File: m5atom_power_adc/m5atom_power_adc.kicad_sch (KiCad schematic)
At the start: 68 parts, among them J101 USB_C_Receptacle_USB2.0_16P, J102 Conn_01x04_Pin, J103 SubBatt, J104 MainBatt, J105 I2C, J106 Shunt, Q101 AO3401A, Q102 MMBT2222A, Q103 AO3401A, SW101 Boot, SW102 Reset, SW103 Btn0, SW104 Btn1, U101 LM2596S-5, U102 AMS1117-3.3, U103 ESP32-S3-MINI-1, U104 AMS1117-3.3, U105 LTC2944, U106 ADS1115IDGS, U108 INA228

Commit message: chore: Grove LED色変更・リレー抵抗を680Ω 500mWに変更・INA228品番更新
Co-Authored-By: Claude Sonnet 4.6 <noreply@anthropic.com>
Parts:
- C112: LCSC C5199872 -> C14663
- R104: value 1k -> 200; LCSC C21190 -> C8218
- U108: LCSC C2862904 -> C2887910
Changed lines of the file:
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@@
 			)
 		)
-		(property "LCSC" "C2862904"
+		(property "LCSC" "C2887910"
 			(at 341.63 45.72 0)
 			(effects
@@
 			)
 		)
-		(property "Value" "1k"
+		(property "Value" "200"
 			(at 132.08 39.37 90)
 			(effects
@@
 			)
 		)
-		(property "LCSC" "C21190"
+		(property "LCSC" "C8218"
 			(at 132.08 41.91 90)
 			(effects
@@
 			)
 		)
-		(property "LCSC" "C5199872"
+		(property "LCSC" "C14663"
 			(at 363.22 34.29 0)
 			(effects

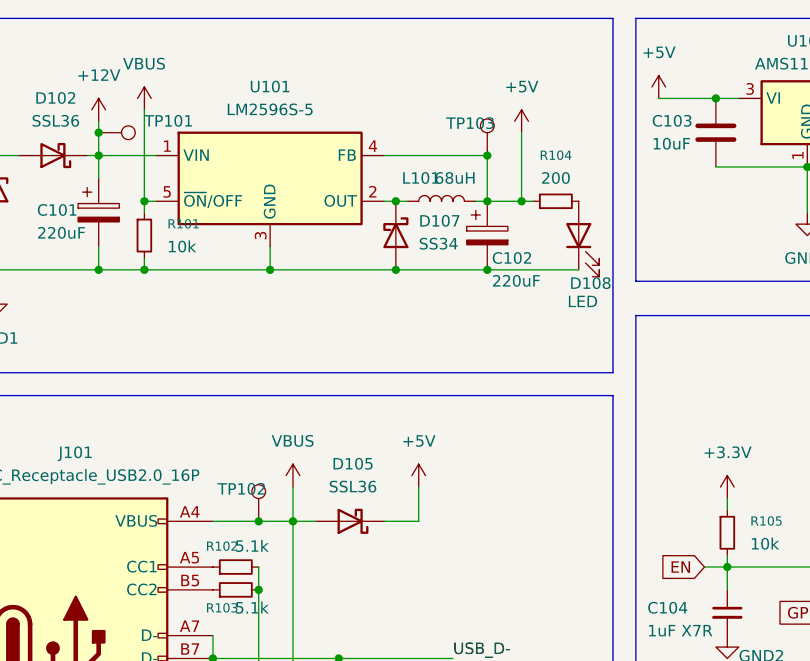
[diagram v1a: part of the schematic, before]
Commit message: feat: m5atom_power_adc 回路・PCB を更新
KiCad 上で行った回路設計・PCB レイアウト変更を反映。
変更内容の詳細は KiCad 上で差分を確認すること。

Co-Authored-By: Claude Sonnet 4.6 <noreply@anthropic.com>
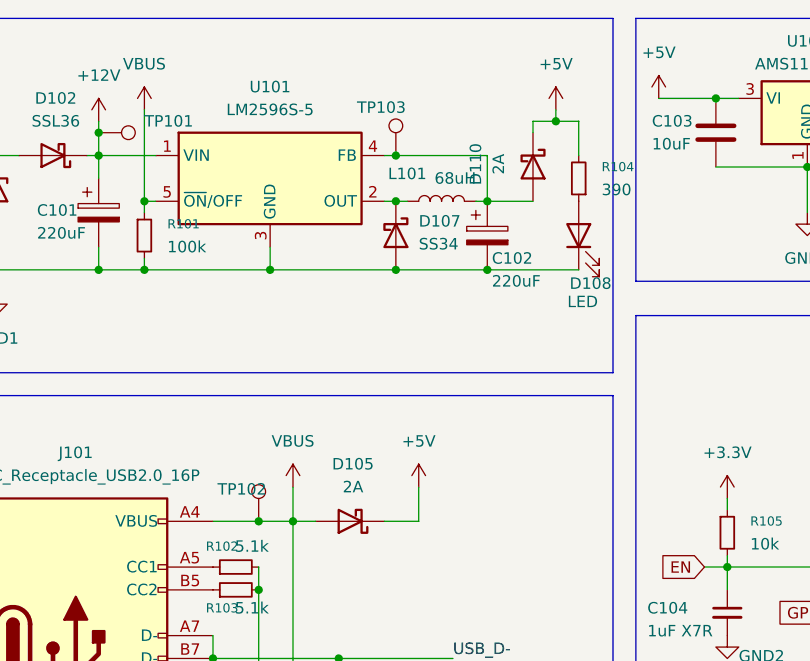
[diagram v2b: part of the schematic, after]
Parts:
- added D110: 2A, Diode_SMD:D_SOD-123F, symbol Device:D_Schottky
- D105: value SSL36 -> 2A; footprint Diode_SMD:D_SMA -> Diode_SMD:D_SOD-123F; LCSC C28646286 -> C496544
- R101: value 10k -> 100k; footprint Resistor_SMD:R_0402_1005Metric -> Resistor_SMD:R_0603_1608Metric; LCSC C2906862 -> C25803
- R102, R103: LCSC C2907045 -> C23186
- R104: value 200 -> 390; LCSC C8218 -> C23151
- R105, R108, R109, R111, R112, R113: footprint Resistor_SMD:R_0402_1005Metric -> Resistor_SMD:R_0603_1608Metric; LCSC C2906862 -> C25804
- R106: LCSC C2906981 -> C25803
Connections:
- net +5V: now also R104.2, D110.1 (K); no longer C102.1, L101.2, R104.1, TP103.1, U101.4 (FB)
- net at D108.2 (A): now also R104.1; no longer R104.2
- new net: C102.1, D110.2 (A), L101.2, TP103.1, U101.4 (FB)
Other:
- moved on the sheet: R104, TP103

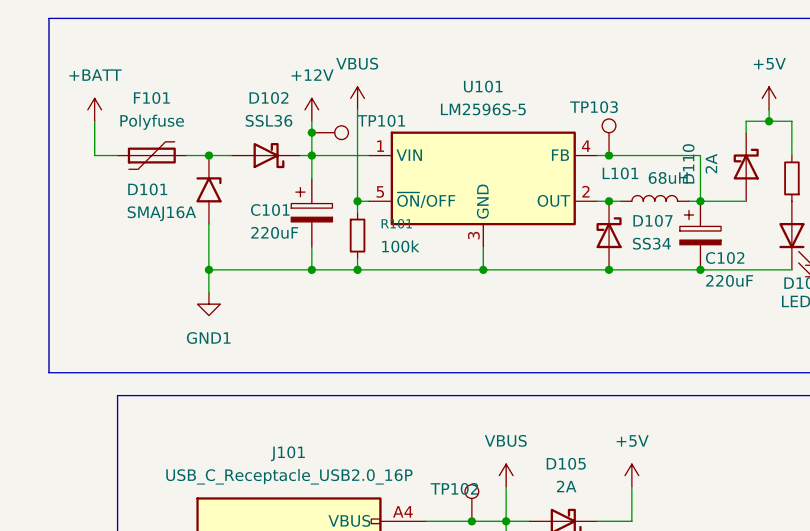
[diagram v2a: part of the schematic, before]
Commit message: fix: R1を100kΩから1kΩに変更（SBD逆方向漏れによる/EN誤動作対策）
SBDの逆方向電流はVR=5V付近でも最大500μAに達するフラット特性のため、
100kΩではV_/EN=5Vとなり/ENしきい値を超えてDCDCが発振する。
1kΩに変更することでV_/EN≤0.5V（25°C）を確保。
LCSC部品番号をC25803→C21190に更新。

Co-Authored-By: Claude Sonnet 4.6 <noreply@anthropic.com>
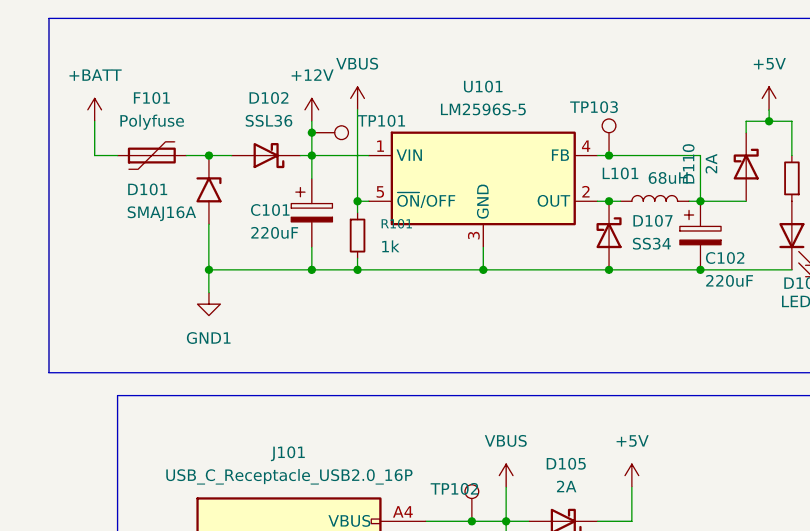
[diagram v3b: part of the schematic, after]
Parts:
- R101: value 100k -> 1k; LCSC C25803 -> C21190
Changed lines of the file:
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@@
 			)
 		)
-		(property "Value" "100k"
+		(property "Value" "1k"
 			(at 88.9 46.9899 0)
 			(effects
@@
 			)
 		)
-		(property "LCSC" "C25803"
+		(property "LCSC" "C21190"
 			(at 86.36 45.72 0)
 			(effects

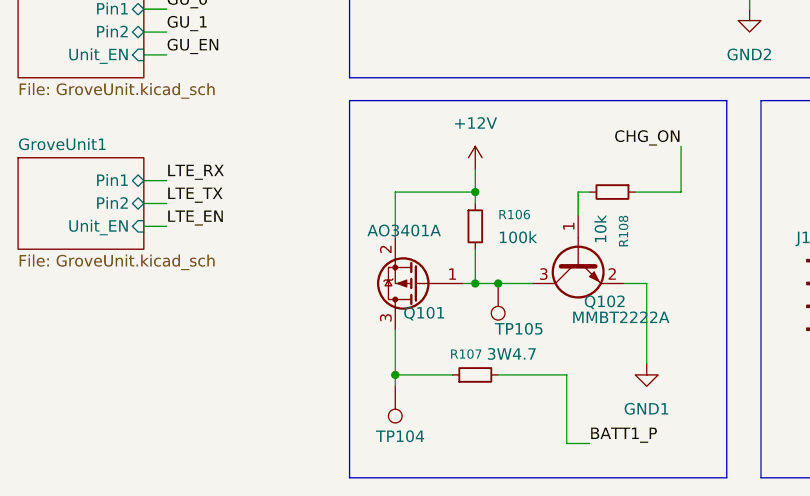
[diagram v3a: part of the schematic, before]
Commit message: feat: 緊急充電回路をバイポーラトランジスタ構成に変更
P-ch MOSFET（AO3401A）をPNPトランジスタに置き換え、ボディダイオードによる
逆電流を防止。ベース電流制限抵抗（R114 470Ω）を追加しQ102の過熱を防ぐ。

Co-Authored-By: Claude Sonnet 4.6 <noreply@anthropic.com>
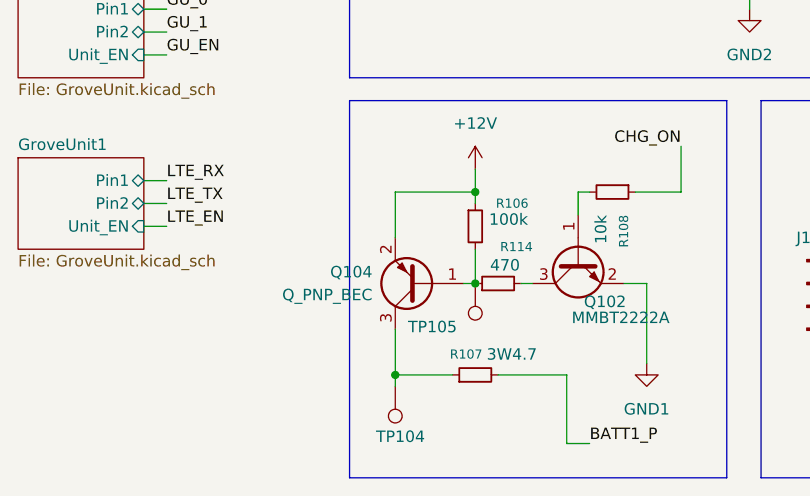
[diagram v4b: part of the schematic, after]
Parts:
- removed Q101: AO3401A, Package_TO_SOT_SMD:SOT-23, symbol Transistor_FET:AO3401A
- added Q104: Q_PNP_BEC, Package_TO_SOT_SMD:SOT-23, symbol Transistor_BJT:Q_PNP_BEC
- added R114: 470, Resistor_SMD:R_0603_1608Metric, symbol Device:R_Small
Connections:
- net +12V: now also Q104.2 (E)
- net at R106.2, TP105.1: now also Q104.1 (B), R114.1; no longer Q102.3 (C)
- net at R107.1, TP104.1: now also Q104.3 (C)
- new net: Q102.3 (C), R114.2
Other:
- moved on the sheet: TP105

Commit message: chore: m5atom_power_adc LCSC 品番を更新
Co-Authored-By: Claude Sonnet 4.6 <noreply@anthropic.com>
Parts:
- Q104: LCSC C8326 -> C7420371
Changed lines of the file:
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@@
 			)
 		)
-		(property "LCSC" "C8326"
+		(property "LCSC" "C7420371"
 			(at 148.59 171.45 0)
 			(effects

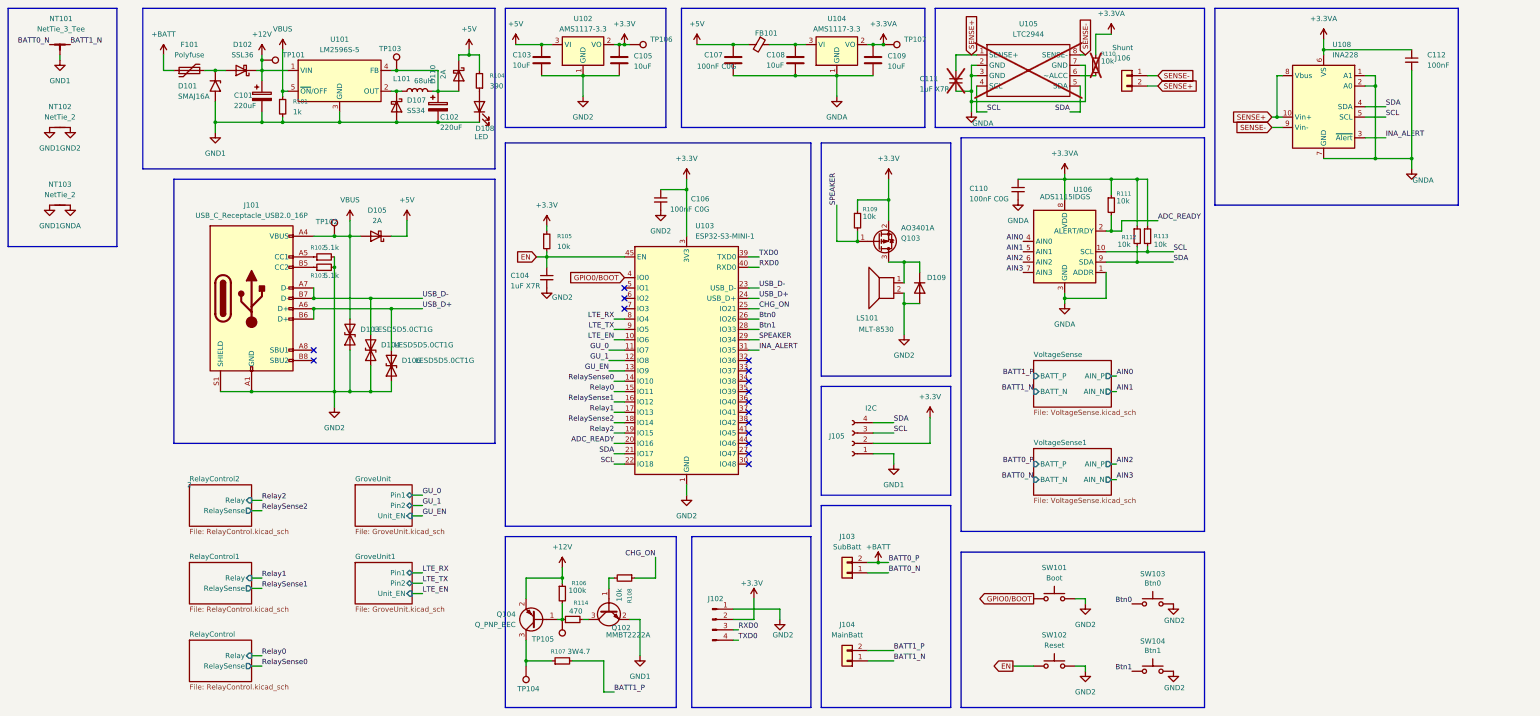
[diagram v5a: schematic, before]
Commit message: feat(m5atom_power_adc): 逆極性保護を理想ダイオード(LM73100)に置き換え、電源スイッチ＆自己保持回路を追加（作業途中）
- LM73100用カスタム記号・フットプリント(VQFN-10-HR)を追加
- 電源回路をサブシートに分離(power.kicad_sch)
- PCBレイアウト更新

Co-Authored-By: Claude Sonnet 4.6 <noreply@anthropic.com>
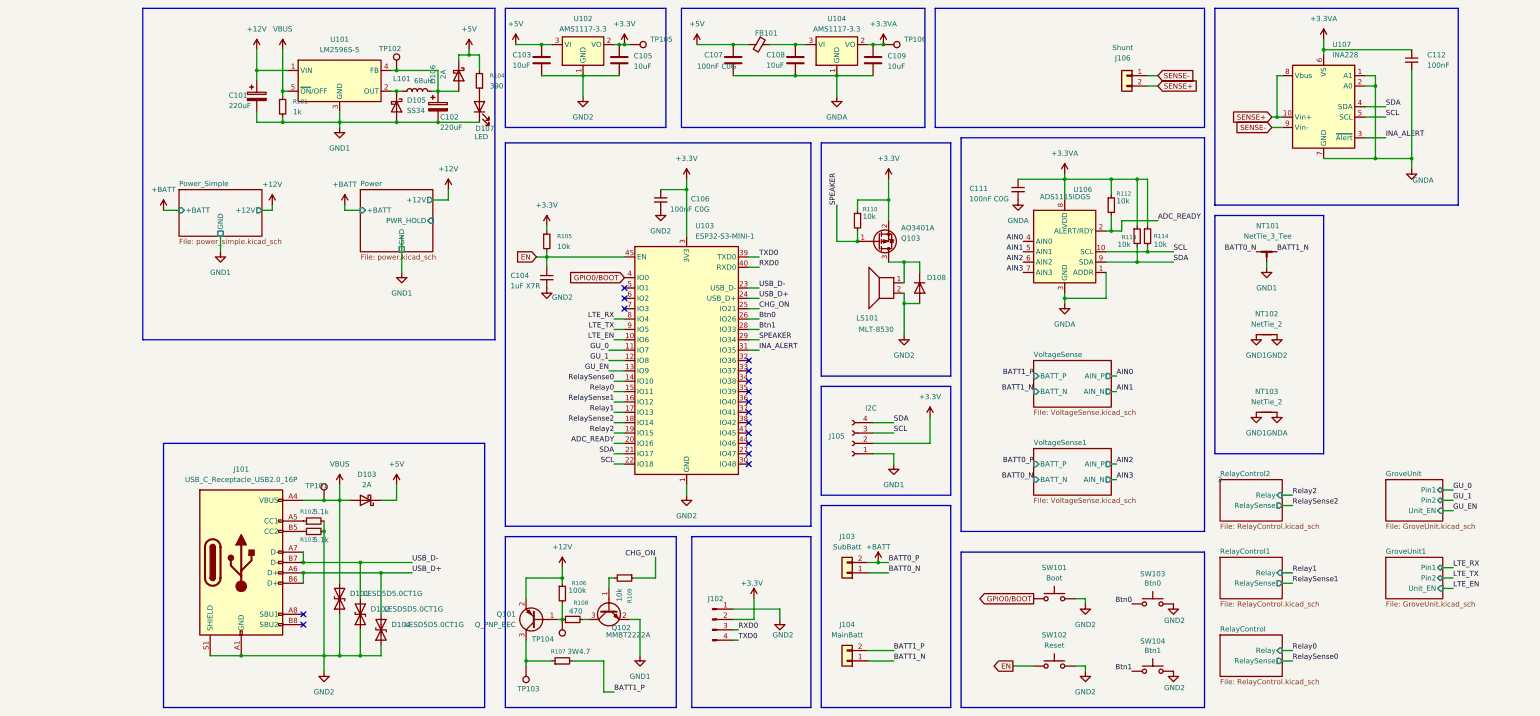
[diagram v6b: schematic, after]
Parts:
- removed C111: 1uF X7R, Capacitor_SMD:C_0603_1608Metric, symbol Device:C_Small
- removed D101: SMAJ16A, Diode_SMD:D_SMB, symbol Diode:SMAJ16A
- removed D102: SSL36, Diode_SMD:D_SMA, symbol Device:D_Schottky
- removed F101: Polyfuse, Fuse:Fuse_1812_4532Metric, symbol Device:Polyfuse
- removed R110: 10k, Resistor_SMD:R_0402_1005Metric, symbol Device:R_Small
- removed TP101: TestPoint, TestPoint:TestPoint_Pad_D1.5mm, symbol Connector:TestPoint
- removed U105: LTC2944, Package_DFN_QFN:DFN-8-1EP_3x3mm_P0.5mm_EP1.65x2.38mm, symbol 000_my:LTC2944
- renumbered C110 to C111, D103 to D101, D104 to D102, D105 to D103, D106 to D104, D107 to D105, D110 to D106, D108 to D107, D109 to D108, Q104 to Q101, R114 to R108, R108 to R109, R109 to R110, R111 to R112, R112 to R113, R113 to R114, TP102 to TP101, TP103 to TP102, TP104 to TP103, TP105 to TP104, TP106 to TP105, TP107 to TP106, U108 to U107
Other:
- added sheet Power (power.kicad_sch)
- added sheet Power_Simple (power_simple.kicad_sch)
- moved on the sheet: C101, D101, D102, D103, D104, J101, NT101, NT102, NT103, R102, R103, TP101

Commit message: feat(m5atom_power_adc): リレー状態検出をアナログ分圧からI2C入力に変更
- 分圧抵抗(R201/R202/R301/R302/R401/R402)とRelaySenseラベルを削除
- I2Cコネクタ(J107/J108)を追加、GP2/GP3/GP11/GP12・PWR_HOLDラベルを追加
- +12VAラベルを+12VRAWにリネーム
- ネットクラスの配線幅プリセットに1.0mmを追加
- PCBのネット再割当て・DRC警告を解消

Co-Authored-By: Claude Sonnet 5 <noreply@anthropic.com>
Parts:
- added J107, J108: I2C, 000_Local:HY2.0-4PZZ, symbol Connector:Conn_01x04_Socket
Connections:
- net RelaySense2 is gone; now on net Relay1: U103.18 (IO14)
- net +3.3V: now also J107.2 (Pin_2), J108.2 (Pin_2)
- net GND1: now also J108.1 (Pin_1)
- net GND2: now also J107.1 (Pin_1)
- net Relay0: now also U103.17 (IO13); no longer U103.15 (IO11)
- net Relay1: no longer U103.17 (IO13)
- net GP2: now reaches U103.6 (IO2)
- net GP2: now also J108.4 (Pin_4)
- net GP3: now reaches U103.7 (IO3)
- net GP3: now also J108.3 (Pin_3)
- net RelaySense0 renamed PWR_HOLD
- net RelaySense1 renamed GP12
- net GP12: now also J107.4 (Pin_4)
- new net GP11: J107.3 (Pin_3), U103.15 (IO11)
- no-connect marks 16 -> 14
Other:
- sheet RelayControl ports: added none; removed RelaySense
- sheet RelayControl1 ports: added none; removed RelaySense
- sheet RelayControl2 ports: added none; removed RelaySense

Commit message: refactor(m5atom_power_adc): Grove Unitのネットラベルをシルク表記に統一
- LTE_RX/TX/EN・GU_0/1/ENをGU1_0/1/EN・GU0_0/1/ENにリネーム
- 基板シルクの「GU0」「GU1」表記に合わせ、CIRCUIT.mdの記載と整合させる

Co-Authored-By: Claude Sonnet 5 <noreply@anthropic.com>
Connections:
- net LTE_EN: no longer U103.10 (IO6)
- net LTE_RX: no longer U103.8 (IO4)
- net LTE_TX: no longer U103.9 (IO5)
- net GU_0 renamed GU1_0
- net GU_1 renamed GU1_1
- net GU_EN renamed GU1_EN
- new net GU0_0: U103.8 (IO4)
- new net GU0_1: U103.9 (IO5)
- new net GU0_EN: U103.10 (IO6)
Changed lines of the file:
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@@
 	(wire
 		(pts
-			(xy 373.38 158.75) (xy 370.84 158.75)
-		)
-		(stroke
-			(width 0)
-			(type default)
-		)
-	)
-	(wire
-		(pts
 			(xy 242.57 86.36) (xy 242.57 83.82)
 		)
@@
 	(wire
 		(pts
+			(xy 370.84 158.75) (xy 373.38 158.75)
+		)
+		(stroke
+			(width 0)
+			(type default)
+		)
+	)
+	(wire
+		(pts
 			(xy 105.41 157.48) (xy 118.11 157.48)
 		)
@@
 	(wire
 		(pts
+			(xy 370.84 163.83) (xy 373.38 163.83)
+		)
+		(stroke
+			(width 0)
+			(type default)
+		)
+	)
+	(wire
+		(pts
 			(xy 238.76 83.82) (xy 234.95 83.82)
 		)
@@
 	(wire
 		(pts
-			(xy 373.38 163.83) (xy 370.84 163.83)
-		)
-		(stroke
-			(width 0)
-			(type default)
-		)
-	)
-	(wire
-		(pts
 			(xy 110.49 160.02) (xy 118.11 160.02)
 		)
@@
 	(wire
 		(pts
-			(xy 373.38 161.29) (xy 370.84 161.29)
-		)
-		(stroke
-			(width 0)
-			(type default)
-		)
-	)
-	(wire
-		(pts
 			(xy 363.22 36.83) (xy 363.22 58.42)
 		)
@@
 	(wire
 		(pts
+			(xy 370.84 161.29) (xy 373.38 161.29)
+		)
+		(stroke
+			(width 0)
+			(type default)
+		)
+	)
+	(wire
+		(pts
 			(xy 330.2 38.1) (xy 331.47 38.1)
 		)
@@
 		)
 	)
+	(label "GU0_EN"
+		(at 167.64 102.87 180)
+		(effects
+			(font
+				(size 1.27 1.27)
+			)
+			(justify right bottom)
+		)
+	)
 	(label "Relay0"
 		(at 334.01 179.07 0)
@@
 		)
 	)
-	(label "GU_EN"
+	(label "GU1_EN"
 		(at 373.38 144.78 0)
 		(effects
@@
 		)
 	)
-	(label "GU_EN"
+	(label "GU1_EN"
 		(at 167.64 110.49 180)
 		(effects
@@
 		)
 	)
-	(label "GU_1"
+	(label "GU0_1"
+		(at 373.38 161.29 0)
+		(effects
+			(font
+				(size 1.27 1.27)
+			)
+			(justify left bottom)
+		)
+	)
+	(label "GU0_EN"
+		(at 373.38 163.83 0)
+		(effects
+			(font
+				(size 1.27 1.27)
+			)
+			(justify left bottom)
+		)
+	)
+	(label "GU1_1"
 		(at 167.64 107.95 180)
 		(effects
@@
 		)
 	)
-	(label "LTE_RX"
-		(at 167.64 97.79 180)
+	(label "Btn1"
+		(at 294.64 184.15 180)
 		(effects
 			(font
@@
 		)
 	)
-	(label "Btn1"
-		(at 294.64 184.15 180)
+	(label "CHG_ON"
+		(at 203.2 95.25 0)
 		(effects
 			(font
 				(size 1.27 1.27)
 			)
-			(justify right bottom)
+			(justify left bottom)
 		)
 	)
-	(label "CHG_ON"
-		(at 203.2 95.25 0)
+	(label "GU0_1"
+		(at 167.64 100.33 180)
 		(effects
 			(font
 				(size 1.27 1.27)
 			)
-			(justify left bottom)
+			(justify right bottom)
 		)
 	)
@@
 	)
 	(label "LTE_RX"
-		(at 373.38 158.75 0)
+		(at 384.81 158.75 0)
 		(effects
 			(font
@@
 		)
 	)
-	(label "LTE_TX"
-		(at 167.64 100.33 180)
-		(effects
-			(font
-				(size 1.27 1.27)
-			)
-			(justify right bottom)
-		)
-	)
 	(label "AIN0"
 		(at 267.97 78.74 180)
@@
 		)
 	)
-	(label "GU_0"
+	(label "GU1_0"
 		(at 167.64 105.41 180)
 		(effects
@@
 		)
 	)
-	(label "GP12"
-		(at 119.38 113.03 0)
+	(label "GU0_0"
+		(at 373.38 158.75 0)
 		(effects
 			(font
@@
 		)
 	)
-	(label "SCL"
-		(at 356.87 48.26 0)
+	(label "GP12"
+		(at 119.38 113.03 0)
 		(effects
 			(font
@@
 		)
 	)
-	(label "USB_D+"
-		(at 203.2 92.71 0)
+	(label "SCL"
+		(at 356.87 48.26 0)
 		(effects
 			(font
@@
 		)
 	)
-	(label "LTE_EN"
-		(at 167.64 102.87 180)
+	(label "USB_D+"
+		(at 203.2 92.71 0)
 		(effects
 			(font
 				(size 1.27 1.27)
 			)
-			(justify right bottom)
+			(justify left bottom)
 		)
 	)
@@
 		)
 	)
+	(label "GU0_0"
+		(at 167.64 97.79 180)
+		(effects
+			(font
+				(size 1.27 1.27)
+			)
+			(justify right bottom)
+		)
+	)
 	(label "BATT0_P"
 		(at 270.51 133.35 180)
@@
 	)
 	(label "LTE_EN"
-		(at 373.38 163.83 0)
+		(at 384.81 163.83 0)
 		(effects
 			(font
@@
 		)
 	)
-	(label "GU_1"
+	(label "GU1_1"
 		(at 373.38 142.24 0)
 		(effects
@@
 		)
 	)
-	(label "GU_0"
+	(label "GU1_0"
 		(at 373.38 139.7 0)
 		(effects
@@
 	)
 	(label "LTE_TX"
-		(at 373.38 161.29 0)
+		(at 384.81 161.29 0)
 		(effects
 			(font
